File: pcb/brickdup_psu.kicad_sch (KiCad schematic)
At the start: 22 parts, among them J1 VBAT/GND in, J2 5V/SENSE/GND, U1 MP9486A

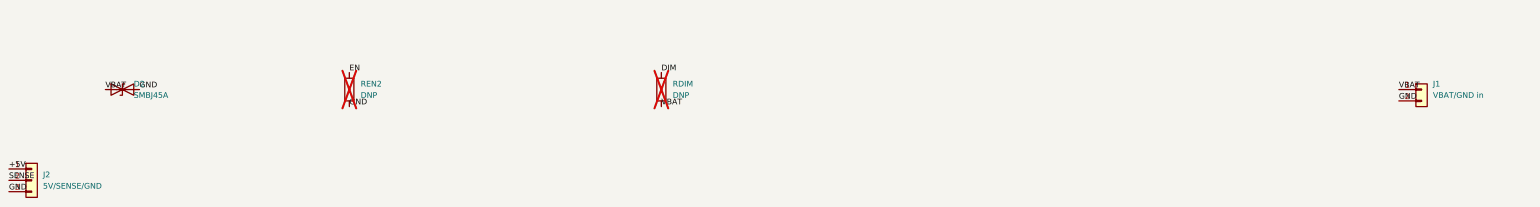
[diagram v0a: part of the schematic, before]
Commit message: pcb: JST-PH connectors (J1/J2) + more LEMO clearance
Switch board I/O to JST-PH 2.0mm SMD side-entry connectors so the board is
plug-in/serviceable and stays single-side SMD for JLC:
- J1 (S2B-PH-SM4-TB): VBAT/GND from the LEMO (crimp cable = no solder).
- J2 (S3B-PH-SM4-TB): 5V/SENSE(GPIO7)/GND to the Heltec (pigtail; the Heltec's
  3 pads remain the one unavoidable solder point since it's a bare module).
Schematic/BOM/outline/render updated; ERC still electrically clean; gerbers OK.
Placement remains a rough GUI-arrange/route starting point.

Enclosure: add psu_gap_e (board east edge holdback) so J1 + its plug clear the
LEMO's rear cups. Clearance echo now reports 15.6 mm (was 12.6). Compiles clean.

Co-Authored-By: Claude Opus 4.8 <noreply@anthropic.com>
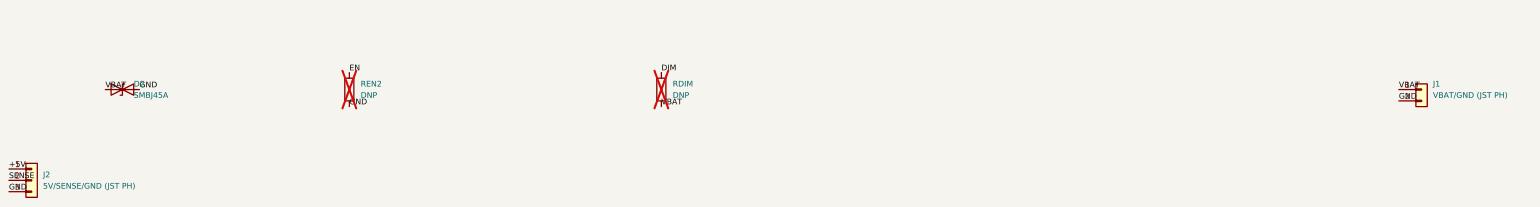
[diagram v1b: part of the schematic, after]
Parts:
- J1: value VBAT/GND in -> VBAT/GND (JST PH); footprint Connector_PinHeader_2.54mm:PinHeader_1x02_P2.54mm_Vertical -> Connector_JST:JST_PH_S2B-PH-SM4-TB_1x02-1MP_P2.00mm_Horizontal
- J2: value 5V/SENSE/GND -> 5V/SENSE/GND (JST PH); footprint Connector_PinHeader_2.54mm:PinHeader_1x03_P2.54mm_Vertical -> Connector_JST:JST_PH_S3B-PH-SM4-TB_1x03-1MP_P2.00mm_Horizontal
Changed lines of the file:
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@@
     (exclude_from_sim no) (in_bom yes) (on_board yes) (dnp no)
     (property "Reference" "J1" (at 353.06 148.59 0) (effects (font (size 1.27 1.27)) (justify left)))
-    (property "Value" "VBAT/GND in" (at 353.06 151.13000000000002 0) (effects (font (size 1.27 1.27)) (justify left)))
-    (property "Footprint" "Connector_PinHeader_2.54mm:PinHeader_1x02_P2.54mm_Vertical" (at 350.52 149.86 0) (effects (font (size 1.27 1.27)) (hide yes)))
+    (property "Value" "VBAT/GND (JST PH)" (at 353.06 151.13000000000002 0) (effects (font (size 1.27 1.27)) (justify left)))
+    (property "Footprint" "Connector_JST:JST_PH_S2B-PH-SM4-TB_1x02-1MP_P2.00mm_Horizontal" (at 350.52 149.86 0) (effects (font (size 1.27 1.27)) (hide yes)))
     (property "Datasheet" "" (at 350.52 149.86 0) (effects (font (size 1.27 1.27)) (hide yes)))
     (pin "1")
@@
     (exclude_from_sim no) (in_bom yes) (on_board yes) (dnp no)
     (property "Reference" "J2" (at 41.91 168.91 0) (effects (font (size 1.27 1.27)) (justify left)))
-    (property "Value" "5V/SENSE/GND" (at 41.91 171.45000000000002 0) (effects (font (size 1.27 1.27)) (justify left)))
-    (property "Footprint" "Connector_PinHeader_2.54mm:PinHeader_1x03_P2.54mm_Vertical" (at 39.37 170.18 0) (effects (font (size 1.27 1.27)) (hide yes)))
+    (property "Value" "5V/SENSE/GND (JST PH)" (at 41.91 171.45000000000002 0) (effects (font (size 1.27 1.27)) (justify left)))
+    (property "Footprint" "Connector_JST:JST_PH_S3B-PH-SM4-TB_1x03-1MP_P2.00mm_Horizontal" (at 39.37 170.18 0) (effects (font (size 1.27 1.27)) (hide yes)))
     (property "Datasheet" "" (at 39.37 170.18 0) (effects (font (size 1.27 1.27)) (hide yes)))
     (pin "1")

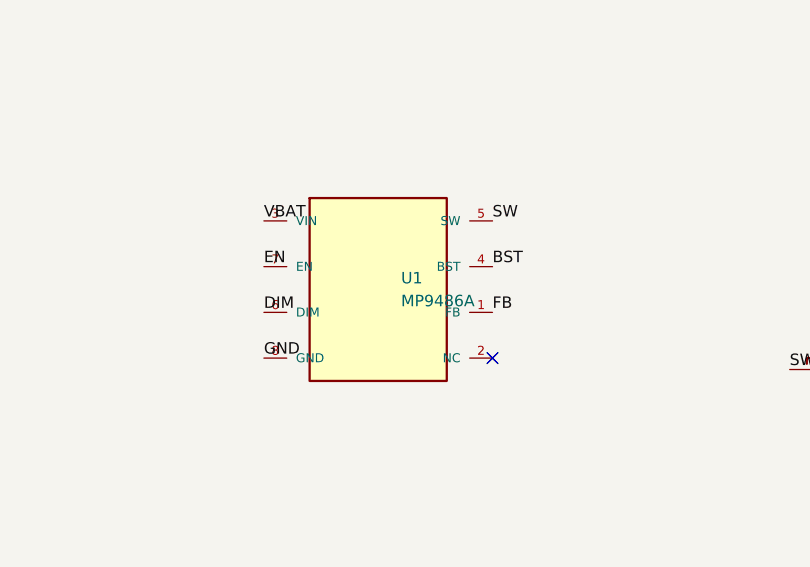
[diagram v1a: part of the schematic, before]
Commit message: pcb: auto-route the board (freerouting) + JLCPCB fab outputs
Full scripted place-and-route pipeline, all reproducible:
  gen_kicad.py -> gen_pcb.py (separation-solver placement, 0 pad overlaps)
  -> export_dsn.py (zones stripped) -> freerouting v2 -> apply_route.py
  (import SES, normalize vias to 0.3/0.6, hide silk refs, fill GND pours).

Result: 40x20 2-layer board, fully placed and **fully routed** -- 0 unconnected,
0 shorts. U1 exposed pad tied to GND (added EP pin to the symbol; grounded by the
top pour). GND poured both layers; copper-to-edge rule 0.3 mm (JLC-safe).
Remaining DRC (~30) is cosmetic silk + a few courtyard/edge/thermal warnings,
documented in README sec 8 -- no opens/shorts.

Adds fab/ with gerbers + zip + CPL + BOM ready to upload to JLCPCB, a 3D render
(docs/pcb_routed_3d.png), and a beginner "Opening it in KiCad" guide.

Co-Authored-By: Claude Opus 4.8 <noreply@anthropic.com>
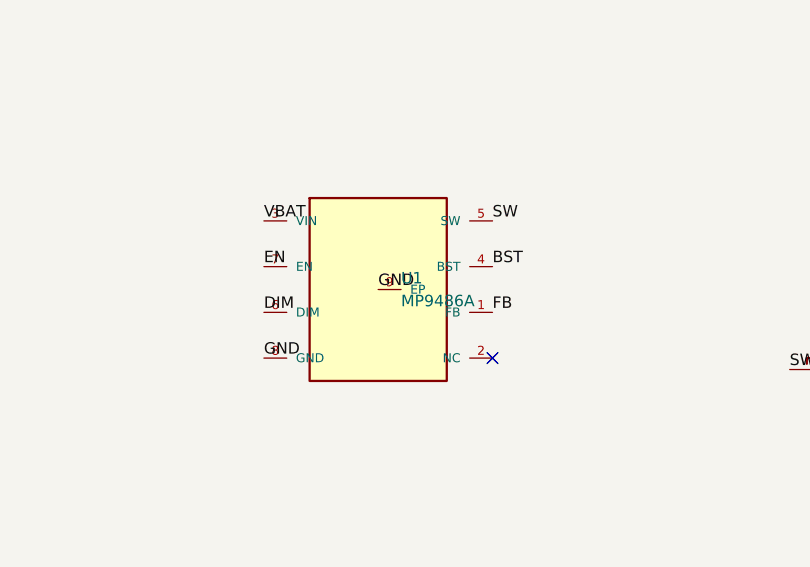
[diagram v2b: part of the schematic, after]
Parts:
- U1: footprint Package_SO:SOIC-8-1EP_3.9x4.9mm_P1.27mm_EP2.41x3.3mm_ThermalVias -> Package_SO:SOIC-8-1EP_3.9x4.9mm_P1.27mm_EP2.41x3.3mm
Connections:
- net GND: now also U1.9 (EP)
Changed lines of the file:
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@@
     (property "Reference" "U1" (at 162.56 109.22 0) (effects (font (size 1.27 1.27)) (justify left)))
     (property "Value" "MP9486A" (at 162.56 111.75999999999999 0) (effects (font (size 1.27 1.27)) (justify left)))
-    (property "Footprint" "Package_SO:SOIC-8-1EP_3.9x4.9mm_P1.27mm_EP2.41x3.3mm_ThermalVias" (at 160.02 110.49 0) (effects (font (size 1.27 1.27)) (hide yes)))
+    (property "Footprint" "Package_SO:SOIC-8-1EP_3.9x4.9mm_P1.27mm_EP2.41x3.3mm" (at 160.02 110.49 0) (effects (font (size 1.27 1.27)) (hide yes)))
     (property "Datasheet" "" (at 160.02 110.49 0) (effects (font (size 1.27 1.27)) (hide yes)))
     (pin "3")
@@
     (pin "1")
     (pin "2")
+    (pin "9")
     (instances
       (project "brickdup_psu"
@@
     (effects (font (size 1.27 1.27)) (justify left bottom))
   )
+  (label "GND"
+    (at 160.02 110.49 0)
+    (effects (font (size 1.27 1.27)) (justify left bottom))
+  )

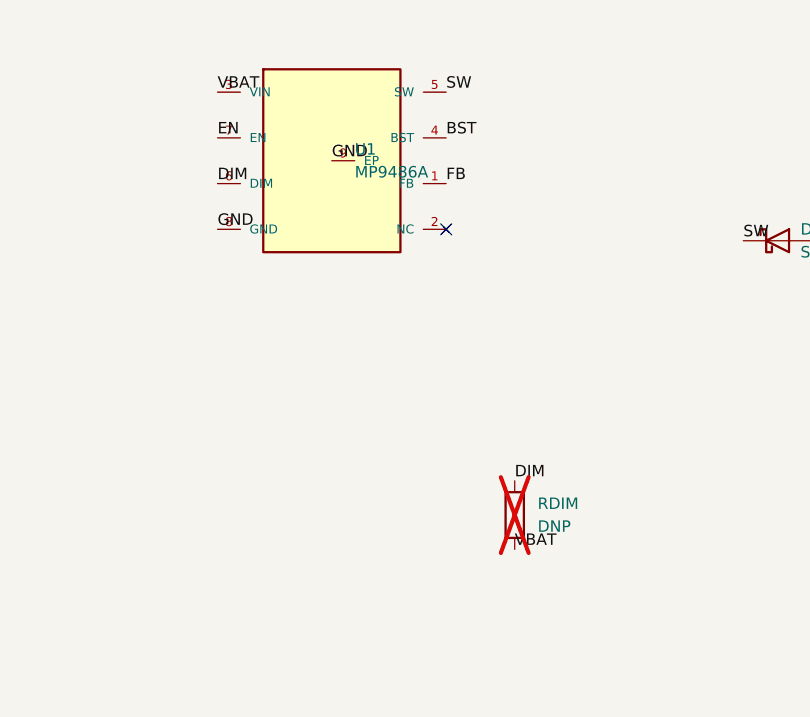
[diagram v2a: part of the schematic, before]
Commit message: pcb: verify MP9486A pinout, tie DIM->EN, ngspice sims
Pre-fab validation pass:
- Pinout VERIFIED against the official MPS datasheet (1 FB, 2 NC, 3 VIN, 4 BST,
  5 SW, 6 DIM, 7 EN, 8 GND, EP->GND) -- matches the symbol/board.
- Datasheet fix: for a non-dimming buck, tie DIM(6) to EN(7). Done -- DIM merged
  into the EN net, the DNP RDIM pull-up removed (21 parts now).
- Re-ran place+route; cleared edge-hugging GND traces (pour carries GND) +
  stitched one re-islanded GND pad. Board: 0 unconnected, 0 shorts, 0 copper-edge;
  17 DRC left = 6 courtyard warnings + cosmetic silk.
- ngspice: divider DC sweep (GPIO7 1.66 V @16.8 V .. 2.50 V @25.2 V, matches math)
  and ideal-buck transient (IL peak ~1.30 A < 1.7 A Isat, dIL ~39%). True output
  ripple / loop stability still need MPSmart + bench (noted in README sec 9).

Regenerated fab/ + 3D render. README/BOM/schematic SVG updated.

Co-Authored-By: Claude Opus 4.8 <noreply@anthropic.com>
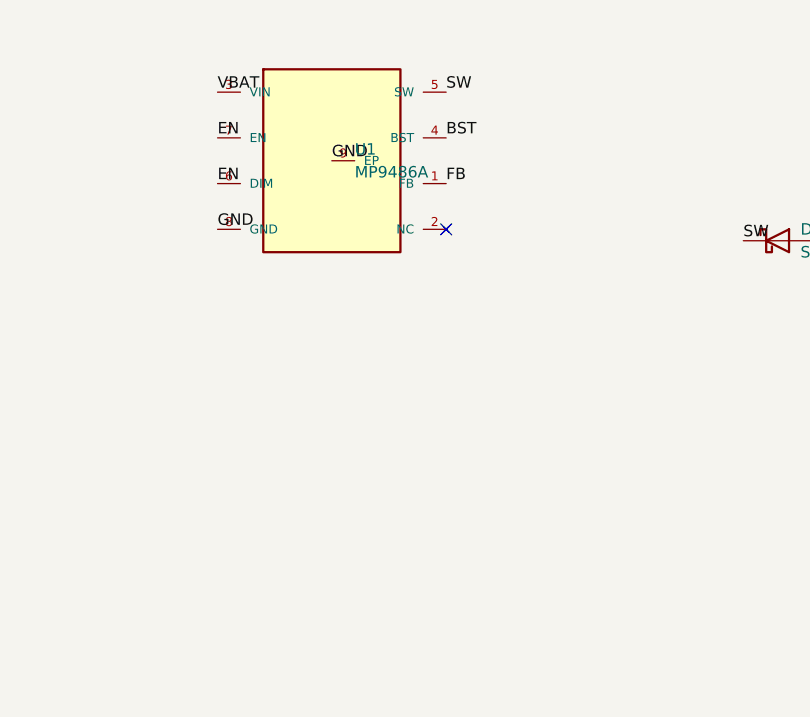
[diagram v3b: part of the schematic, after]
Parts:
- removed RDIM: DNP, Resistor_SMD:R_0402_1005Metric, symbol Device:R
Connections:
- net DIM is gone; now on net EN: U1.6 (DIM)
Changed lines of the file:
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@@
-  (symbol
-    (lib_id "Device:R")
-    (at 180.34 149.86 0)
-    (unit 1)
-    (exclude_from_sim no) (in_bom yes) (on_board yes) (dnp yes)
-    (property "Reference" "RDIM" (at 182.88 148.59 0) (effects (font (size 1.27 1.27)) (justify left)))
-    (property "Value" "DNP" (at 182.88 151.13000000000002 0) (effects (font (size 1.27 1.27)) (justify left)))
-    (property "Footprint" "Resistor_SMD:R_0402_1005Metric" (at 180.34 149.86 0) (effects (font (size 1.27 1.27)) (hide yes)))
-    (property "Datasheet" "" (at 180.34 149.86 0) (effects (font (size 1.27 1.27)) (hide yes)))
-    (pin "1")
-    (pin "2")
-    (instances
-      (project "brickdup_psu"
-        (path "/6e3bc9d9-b743-593a-8e81-87e97b73fbe4" (reference "RDIM") (unit 1))))
-  )
   (symbol
     (lib_id "Device:R")
@@
     (effects (font (size 1.27 1.27)) (justify left bottom))
   )
-  (label "VBAT"
-    (at 180.34 153.67 0)
-    (effects (font (size 1.27 1.27)) (justify left bottom))
-  )
   (label "GND"
     (at 147.32 118.11 0)
@@
   )
   (label "EN"
+    (at 147.32 113.03 0)
+    (effects (font (size 1.27 1.27)) (justify left bottom))
+  )
+  (label "EN"
     (at 110.49 73.66 0)
     (effects (font (size 1.27 1.27)) (justify left bottom))
@@
     (effects (font (size 1.27 1.27)) (justify left bottom))
   )
-  (label "DIM"
-    (at 147.32 113.03 0)
-    (effects (font (size 1.27 1.27)) (justify left bottom))
-  )
-  (label "DIM"
-    (at 180.34 146.05 0)
-    (effects (font (size 1.27 1.27)) (justify left bottom))
-  )

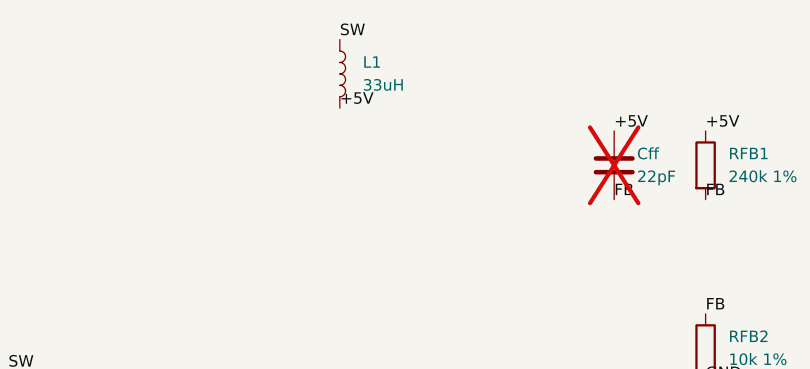
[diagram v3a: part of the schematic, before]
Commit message: pcb: swap L1 to 12mm 3A inductor (CYH127-33UH) + re-route
The previous 7.3mm L1 footprint could only take ~1.2A inductors, which would
saturate at the 1.30A peak. Swap to a real adequate part: SHOU HAN CYH127-33UH
(C2929502, 33uH / 3A) on the matching L_12x12mm_H8mm footprint, and re-run
place+route. Moved the M2 mounting holes to the south band (clear of the J2/J1
connector edges) and the enclosure J2 wire-notch to match J2's new position.

Board: 0 unconnected, 0 shorts (routed the one stranded VBAT pad on B.Cu,
removed GND-pour islands). DRC 34 = cosmetic silk + warnings; note the bigger
inductor crowds the board (11 courtyard-overlap warnings). Enclosure recompiles;
fab/ + render + BOM (L1 = C2929502) regenerated.

Co-Authored-By: Claude Opus 4.8 <noreply@anthropic.com>
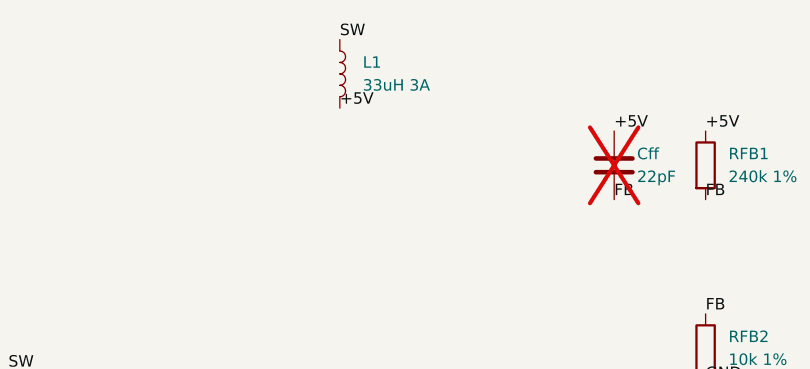
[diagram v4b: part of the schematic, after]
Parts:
- L1: value 33uH -> 33uH 3A; footprint Inductor_SMD:L_7.3x7.3_H4.5 -> Inductor_SMD:L_12x12mm_H8mm
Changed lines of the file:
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@@
     (exclude_from_sim no) (in_bom yes) (on_board yes) (dnp no)
     (property "Reference" "L1" (at 212.09 68.58 0) (effects (font (size 1.27 1.27)) (justify left)))
-    (property "Value" "33uH" (at 212.09 71.11999999999999 0) (effects (font (size 1.27 1.27)) (justify left)))
-    (property "Footprint" "Inductor_SMD:L_7.3x7.3_H4.5" (at 209.55 69.85 0) (effects (font (size 1.27 1.27)) (hide yes)))
+    (property "Value" "33uH 3A" (at 212.09 71.11999999999999 0) (effects (font (size 1.27 1.27)) (justify left)))
+    (property "Footprint" "Inductor_SMD:L_12x12mm_H8mm" (at 209.55 69.85 0) (effects (font (size 1.27 1.27)) (hide yes)))
     (property "Datasheet" "" (at 209.55 69.85 0) (effects (font (size 1.27 1.27)) (hide yes)))
     (pin "1")

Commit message: pcb: switch L1 to CYA0850 (9.2x8mm, 6A) on a custom footprint
Replace the crowding 12.3mm CYH127 with SHOU HAN CYA0850-33UH (C19268648):
33uH, 3A rated / 6A saturation, 9.2x8mm molded -- smaller AND much higher
current margin (6A sat vs 1.30A peak). Added a correct project-local footprint
pcb/brickdup.pretty/L_CYA0850 (2-pad, 9.2x8 land) and taught gen_pcb to load
project footprints.

Re-ran place+route: fully routed, **0 unconnected, 0 shorts**, no isolated
copper, no manual fixups. Courtyard-overlap warnings down 11 -> 7; remaining
31 DRC are cosmetic silk + 7 courtyard warnings. Regenerated fab/ + render;
BOM L1 = C19268648.

Co-Authored-By: Claude Opus 4.8 <noreply@anthropic.com>
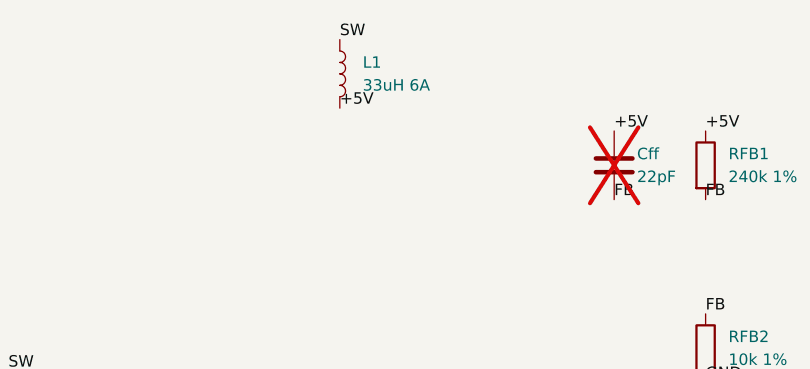
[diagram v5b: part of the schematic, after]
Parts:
- L1: value 33uH 3A -> 33uH 6A; footprint Inductor_SMD:L_12x12mm_H8mm -> brickdup:L_CYA0850
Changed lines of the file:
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@@
     (exclude_from_sim no) (in_bom yes) (on_board yes) (dnp no)
     (property "Reference" "L1" (at 212.09 68.58 0) (effects (font (size 1.27 1.27)) (justify left)))
-    (property "Value" "33uH 3A" (at 212.09 71.11999999999999 0) (effects (font (size 1.27 1.27)) (justify left)))
-    (property "Footprint" "Inductor_SMD:L_12x12mm_H8mm" (at 209.55 69.85 0) (effects (font (size 1.27 1.27)) (hide yes)))
+    (property "Value" "33uH 6A" (at 212.09 71.11999999999999 0) (effects (font (size 1.27 1.27)) (justify left)))
+    (property "Footprint" "brickdup:L_CYA0850" (at 209.55 69.85 0) (effects (font (size 1.27 1.27)) (hide yes)))
     (property "Datasheet" "" (at 209.55 69.85 0) (effects (font (size 1.27 1.27)) (hide yes)))
     (pin "1")
